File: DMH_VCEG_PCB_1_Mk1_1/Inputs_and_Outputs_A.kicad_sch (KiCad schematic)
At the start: 45 parts, among them J1 TS_Jack_6.35mm_Sw, J10 TS_Jack_6.35mm_Sw, J2 TS_Jack_6.35mm_Sw, J200 IDC_02x08, J21 Conn_01x10_PinHeader, J22 Conn_01x10_PinHeader, J23 Conn_01x10_PinHeader, J24 Conn_01x06_PinHeader, J3 TS_Jack_6.35mm_Sw, J4 TS_Jack_6.35mm_Sw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

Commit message: Out R rework ongoing
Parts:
- R197: value 68k -> 100k
- R198: value 100k -> 68k
- R88: value 68K -> 68k
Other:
- note removed: "Must be inverted"
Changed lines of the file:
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@@
 	)
 	(rectangle
-		(start 118.11 187.96)
-		(end 135.89 193.04)
-		(stroke
-			(width 0)
-			(type default)
-		)
-		(fill
-			(type none)
-		)
-	)
-	(rectangle
 		(start 96.52 160.02)
 		(end 140.97 199.39)
@@
 		)
 	)
-	(text "Must be inverted"
-		(exclude_from_sim no)
-		(at 128.016 186.69 0)
-		(effects
-			(font
-				(size 1.27 1.27)
-			)
-		)
-	)
 	(text "PCB 2"
 		(exclude_from_sim no)
@@
 			)
 		)
-		(property "Value" "68K"
+		(property "Value" "68k"
 			(at 119.38 165.1 90)
 			(effects
@@
 			)
 		)
-		(property "Value" "100k"
+		(property "Value" "68k"
 			(at 121.92 194.31 90)
 			(effects
@@
 			)
 		)
-		(property "Value" "68k"
+		(property "Value" "100k"
 			(at 132.08 194.31 90)
 			(effects

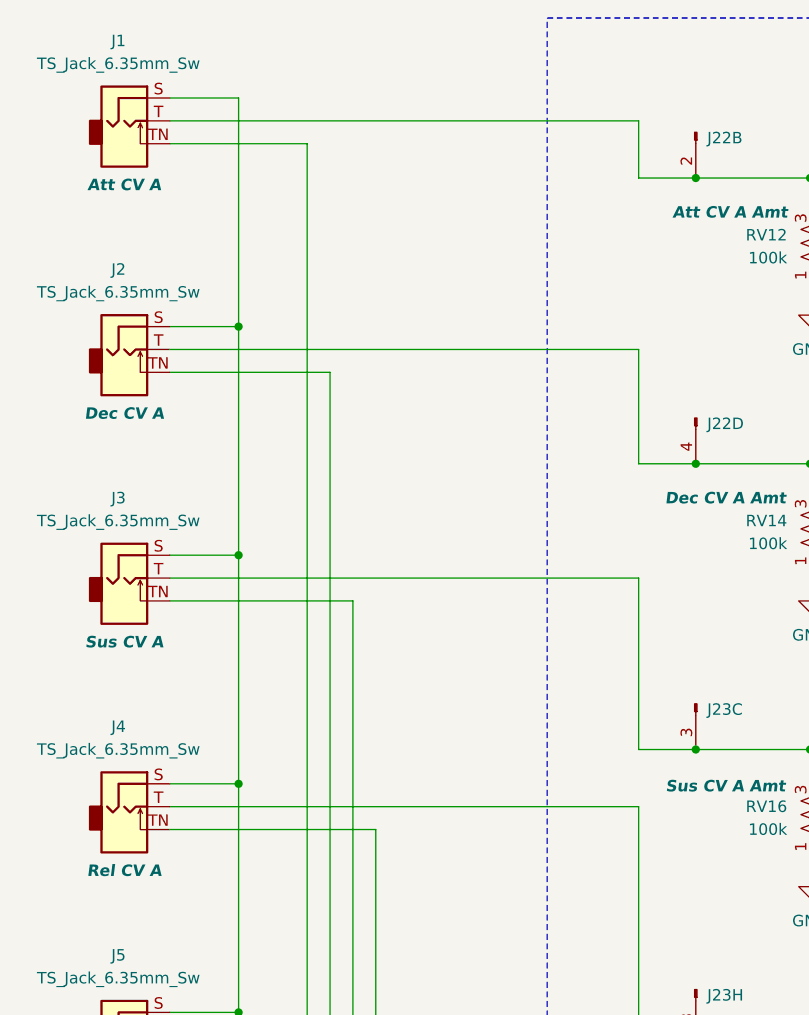
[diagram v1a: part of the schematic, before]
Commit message: Fixed normalled tip routing for CV and Gate
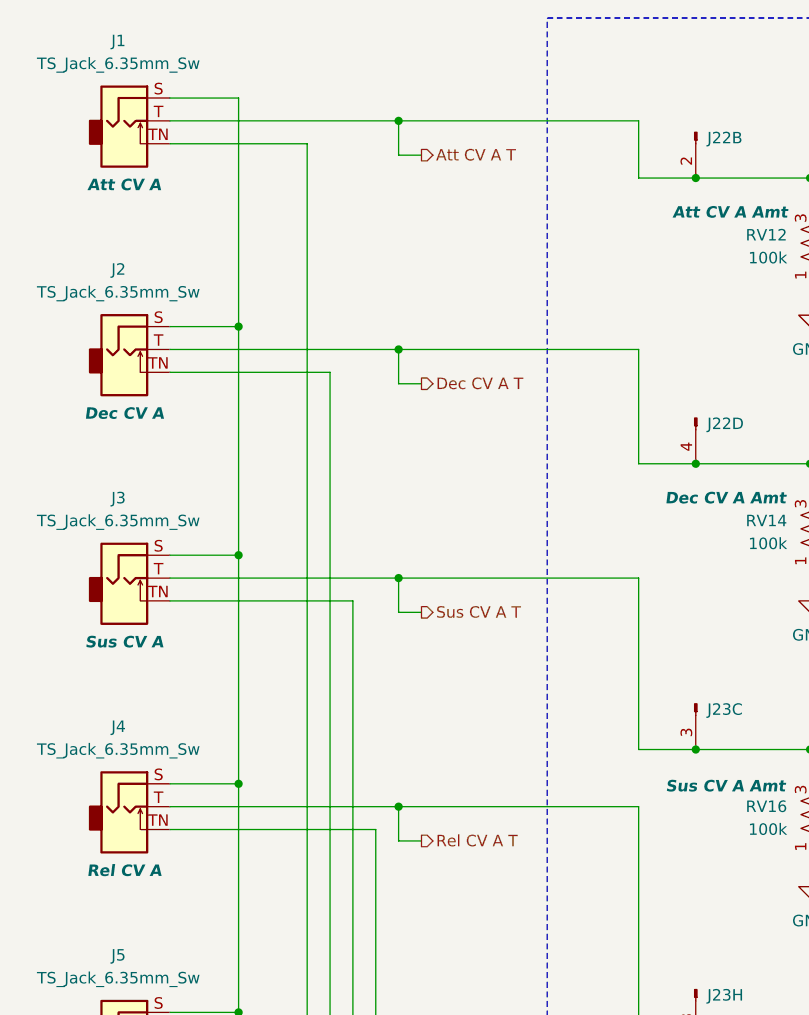
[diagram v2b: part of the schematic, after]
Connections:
- net Dec CV A T: now reaches J2.T, J22.4 (Pin_4), R85.1, RV14.3
- net Rel CV A T: now reaches J23.8 (Pin_8), J4.T, R87.1, RV18.3
- net Sus CV A T: now reaches J23.3 (Pin_3), J3.T, R86.1, RV16.3
- net Att CV A T: now reaches J1.T, J22.2 (Pin_2), R84.1, RV12.3
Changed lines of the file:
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@@
+	)
+	(junction
+		(at 55.88 76.2)
+		(diameter 0)
+		(color 0 0 0 0)
 	)
 	(junction
@@
 	)
 	(junction
+		(at 55.88 50.8)
+		(diameter 0)
+		(color 0 0 0 0)
+	)
+	(junction
 		(at 132.08 228.6)
 		(diameter 0)
@@
 	)
 	(junction
+		(at 55.88 101.6)
+		(diameter 0)
+		(color 0 0 0 0)
+	)
+	(junction
 		(at 38.1 48.26)
 		(diameter 0)
@@
 	(junction
 		(at 101.6 127)
+		(diameter 0)
+		(color 0 0 0 0)
+	)
+	(junction
+		(at 55.88 25.4)
 		(diameter 0)
 		(color 0 0 0 0)
@@
 	(wire
 		(pts
-			(xy 30.48 25.4) (xy 82.55 25.4)
+			(xy 30.48 25.4) (xy 55.88 25.4)
 		)
 		(stroke
@@
 	(wire
 		(pts
-			(xy 30.48 101.6) (xy 82.55 101.6)
+			(xy 30.48 101.6) (xy 55.88 101.6)
 		)
 		(stroke
@@
 	(wire
 		(pts
+			(xy 55.88 25.4) (xy 82.55 25.4)
+		)
+		(stroke
+			(width 0)
+			(type default)
+		)
+	)
+	(wire
+		(pts
 			(xy 50.8 231.14) (xy 50.8 280.67)
 		)
@@
 	(wire
 		(pts
-			(xy 30.48 50.8) (xy 82.55 50.8)
+			(xy 30.48 50.8) (xy 55.88 50.8)
 		)
 		(stroke
@@
 	(wire
 		(pts
+			(xy 55.88 25.4) (xy 55.88 29.21)
+		)
+		(stroke
+			(width 0)
+			(type default)
+		)
+	)
+	(wire
+		(pts
 			(xy 53.34 104.14) (xy 53.34 165.1)
 		)
@@
 	(wire
 		(pts
+			(xy 58.42 29.21) (xy 55.88 29.21)
+		)
+		(stroke
+			(width 0)
+			(type default)
+		)
+	)
+	(wire
+		(pts
 			(xy 115.57 39.37) (xy 115.57 36.83)
 		)
@@
 	(wire
 		(pts
-			(xy 30.48 76.2) (xy 82.55 76.2)
+			(xy 30.48 76.2) (xy 55.88 76.2)
 		)
 		(stroke
@@
 	(wire
 		(pts
+			(xy 58.42 54.61) (xy 55.88 54.61)
+		)
+		(stroke
+			(width 0)
+			(type default)
+		)
+	)
+	(wire
+		(pts
 			(xy 88.9 177.8) (xy 97.79 177.8)
 		)
@@
 	(wire
 		(pts
+			(xy 55.88 76.2) (xy 55.88 80.01)
+		)
+		(stroke
+			(width 0)
+			(type default)
+		)
+	)
+	(wire
+		(pts
 			(xy 111.76 127) (xy 115.57 127)
 		)
@@
 	(wire
 		(pts
+			(xy 55.88 50.8) (xy 55.88 54.61)
+		)
+		(stroke
+			(width 0)
+			(type default)
+		)
+	)
+	(wire
+		(pts
 			(xy 105.41 71.12) (xy 115.57 71.12)
 		)
@@
 	(wire
 		(pts
+			(xy 58.42 105.41) (xy 55.88 105.41)
+		)
+		(stroke
+			(width 0)
+			(type default)
+		)
+	)
+	(wire
+		(pts
 			(xy 109.22 219.71) (xy 109.22 231.14)
 		)
@@
 	(wire
 		(pts
+			(xy 55.88 50.8) (xy 82.55 50.8)
+		)
+		(stroke
+			(width 0)
+			(type default)
+		)
+	)
+	(wire
+		(pts
 			(xy 45.72 27.94) (xy 45.72 172.72)
 		)
@@
 	(wire
 		(pts
+			(xy 55.88 76.2) (xy 82.55 76.2)
+		)
+		(stroke
+			(width 0)
+			(type default)
+		)
+	)
+	(wire
+		(pts
 			(xy 138.43 97.79) (xy 158.75 97.79)
 		)
@@
 	(wire
 		(pts
+			(xy 55.88 101.6) (xy 55.88 105.41)
+		)
+		(stroke
+			(width 0)
+			(type default)
+		)
+	)
+	(wire
+		(pts
 			(xy 60.96 278.13) (xy 60.96 270.51)
 		)
@@
 	(wire
 		(pts
+			(xy 55.88 101.6) (xy 82.55 101.6)
+		)
+		(stroke
+			(width 0)
+			(type default)
+		)
+	)
+	(wire
+		(pts
 			(xy 115.57 63.5) (xy 119.38 63.5)
 		)
@@
 	(wire
 		(pts
+			(xy 58.42 80.01) (xy 55.88 80.01)
+		)
+		(stroke
+			(width 0)
+			(type default)
+		)
+	)
+	(wire
+		(pts
 			(xy 152.4 241.3) (xy 152.4 246.38)
 		)
@@
 			(width 0)
 			(type default)
+		)
+	)
+	(hierarchical_label "Rel CV A T"
+		(shape output)
+		(at 58.42 105.41 0)
+		(effects
+			(font
+				(size 1.27 1.27)
+			)
+			(justify left)
 		)
 	)
@@
 		)
 	)
+	(hierarchical_label "Att CV A T"
+		(shape output)
+		(at 58.42 29.21 0)
+		(effects
+			(font
+				(size 1.27 1.27)
+			)
+			(justify left)
+		)
+	)
 	(hierarchical_label "SG Out A"
 		(shape input)
@@
 		)
 	)
+	(hierarchical_label "Dec CV A T"
+		(shape output)
+		(at 58.42 54.61 0)
+		(effects
+			(font
+				(size 1.27 1.27)
+			)
+			(justify left)
+		)
+	)
 	(hierarchical_label "Rel CV A"
 		(shape output)
@@
 		(effects
 			(font
+				(size 1.27 1.27)
+			)
+			(justify left)
+		)
+	)
+	(hierarchical_label "Sus CV A T"
+		(shape output)
+		(at 58.42 80.01 0)
+		(effects
+			(font
